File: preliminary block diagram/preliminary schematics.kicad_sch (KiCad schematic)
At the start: 14 parts, among them U1 Mixer, U10 Mixer, U11 Mixer, U12 ADP-2-1W, U13 PAT1220-C-1DB, U2 Mixer, U3 ADP-2-1W, U4 ADP-2-1W, U5 HMC513+100MHz oscillator, U6 ADP-2-1W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

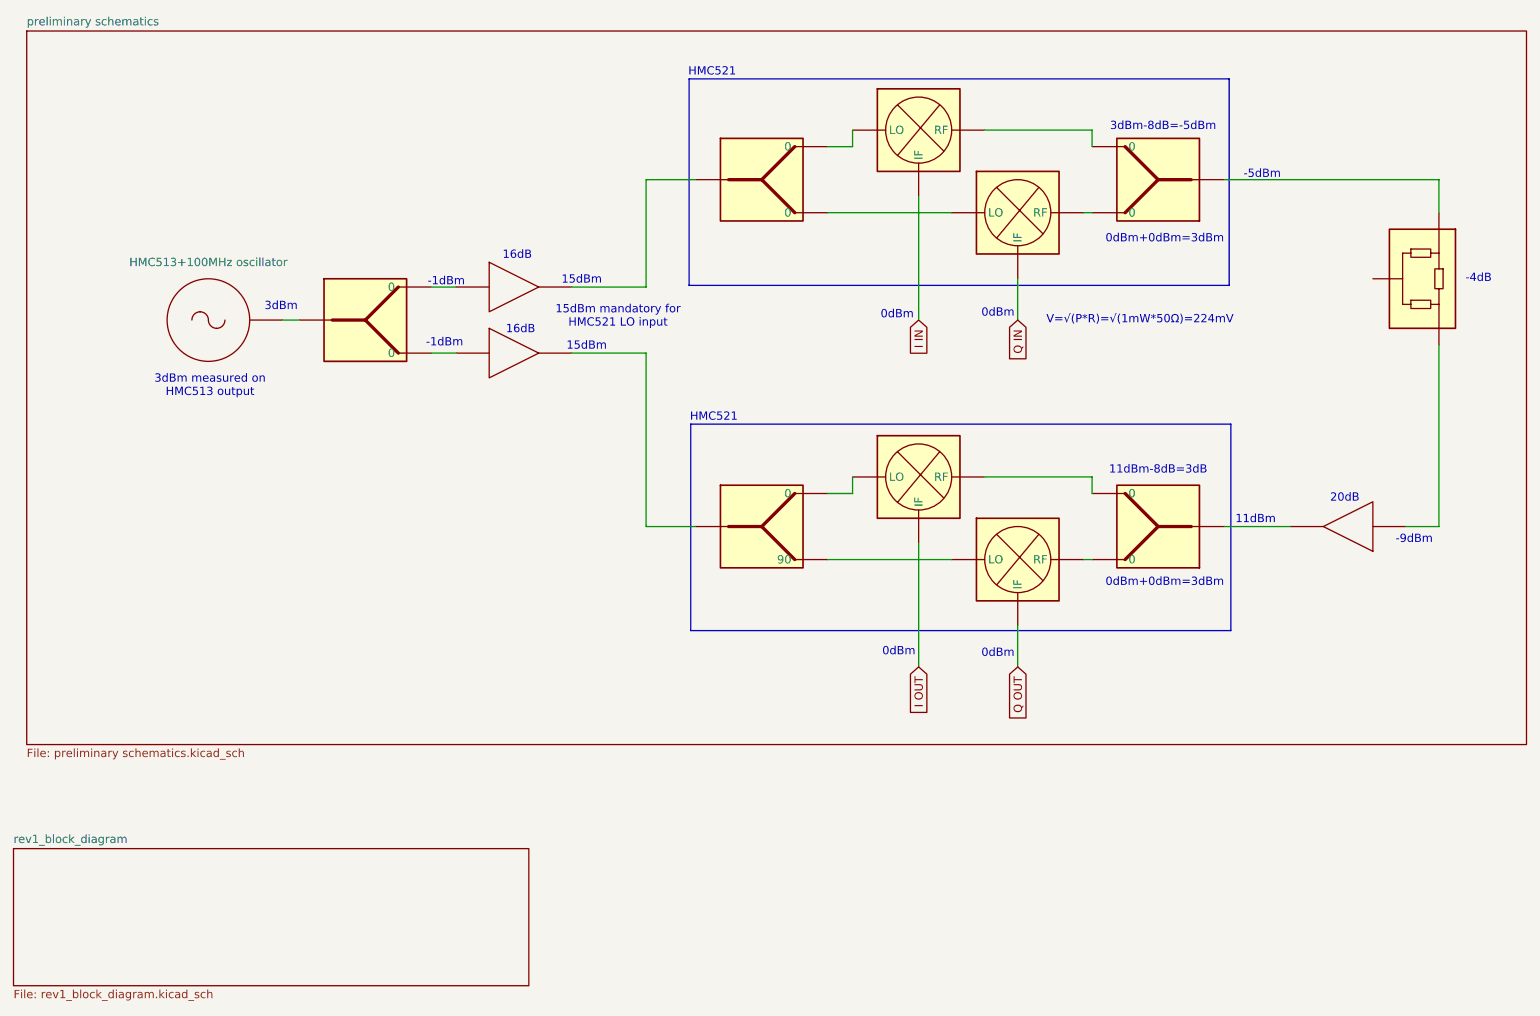
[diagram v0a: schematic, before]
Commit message: new file:   Datasheets/hmc451lp3.pdf
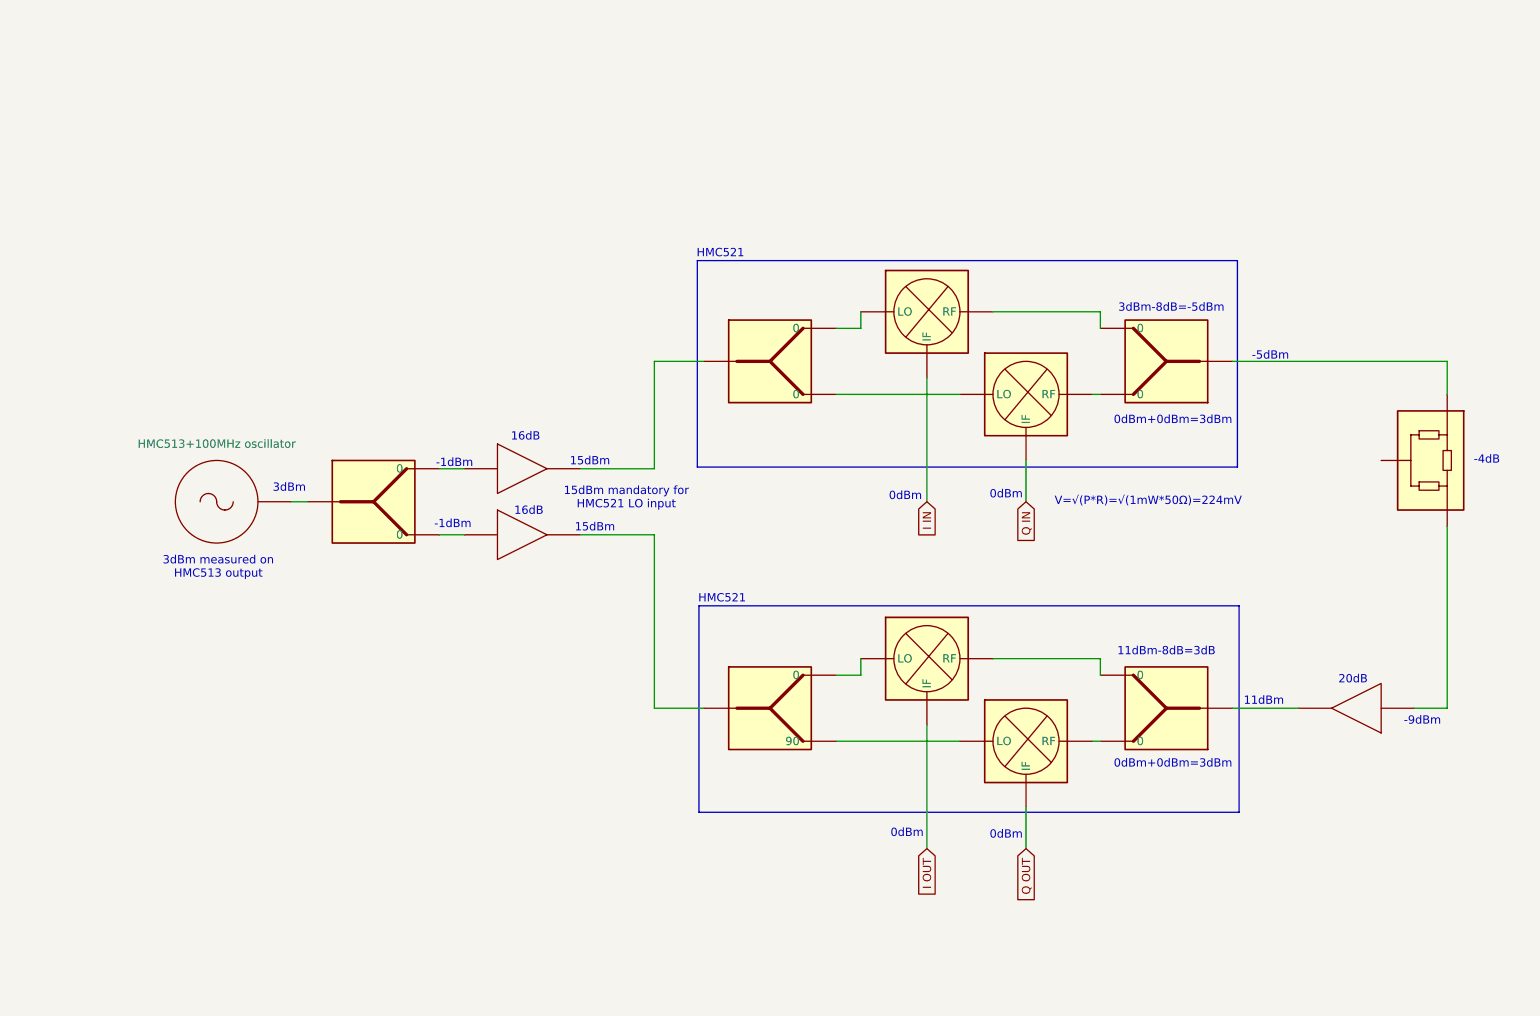
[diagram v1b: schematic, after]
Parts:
- removed U1, U10, U11, U2: Mixer, RF_Mini-Circuits:Mini-Circuits_CD542_LandPatternPL-052, symbol custom_rf_symbols:Mixer
- removed U12, U3, U4, U6, U9: ADP-2-1W, RF_Mini-Circuits:Mini-Circuits_CD636_LandPatternPL-035, symbol RF:ADP-2-1W
- removed U13: PAT1220-C-1DB, RF_Converter:RF_Attenuator_Susumu_PAT1220, symbol RF:PAT1220-C-1DB
- removed U14, U7, U8: ~, symbol custom_rf_symbols:Amplifier
- removed U5: HMC513+100MHz oscillator, symbol custom_rf_symbols:Oscillator
- added U15: HMC513+100MHz oscillator, symbol custom_rf_symbols:Oscillator
- added U16, U19, U20, U25, U26: ADP-2-1W, RF_Mini-Circuits:Mini-Circuits_CD636_LandPatternPL-035, symbol RF:ADP-2-1W
- added U17, U18, U27: ~, symbol custom_rf_symbols:Amplifier
- added U21, U22, U23, U24: Mixer, RF_Mini-Circuits:Mini-Circuits_CD542_LandPatternPL-052, symbol custom_rf_symbols:Mixer
- added U28: PAT1220-C-1DB, RF_Converter:RF_Attenuator_Susumu_PAT1220, symbol RF:PAT1220-C-1DB
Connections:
- net I IN: now also U21.6 (IF)
- net I OUT: now also U22.6 (IF)
- net Q IN: now also U23.6 (IF)
- net Q OUT: now also U24.6 (IF)
- new net: U25.1, U28.1
- new net: U27.1 (IN), U28.2
- new net: U16.3 (0), U17.1 (IN)
- new net: U17.2 (OUT), U19.1
- new net: U15. (outpu), U16.1
- new net: U16.4 (0), U18.1 (IN)
- new net: U26.1, U27.2 (OUT)
- new net: U24.2 (RF), U26.3 (0)
- new net: U20.4 (90), U24.3 (LO)
- new net: U24.4 (GND), U24.5 (GND)
- new net: U21.2 (RF), U25.4 (0)
- new net: U19.3 (0), U21.3 (LO)
- new net: U21.4 (GND), U21.5 (GND)
- new net: U19.4 (0), U23.3 (LO)
- new net: U18.2 (OUT), U20.1
- new net: U22.2 (RF), U26.4 (0)
- new net: U20.3 (0), U22.3 (LO)
- new net: U22.4 (GND), U22.5 (GND)
- new net: U23.2 (RF), U25.3 (0)
- new net: U23.4 (GND), U23.5 (GND)
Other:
- removed sheet preliminary schematics
- removed sheet rev1_block_diagram
